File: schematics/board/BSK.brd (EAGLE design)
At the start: 80 x 80 mm, 58 parts, among them IC2 MAX809REUR, J1 idc_2x5, SW1 RST

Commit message: изменен БСК4
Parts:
- removed R2, R7: 10k, resistor:R0603
- removed U$16: FS8205A, CanCubeSat:FS8205A
- VAR3: device pinheadCS:1X12 -> pinheadCS:1X14
- moved VAR3 111.5 mm to (-80.0, -743.0)
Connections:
- removed net N$4: R2.2, U$16.4
- removed net N$6: R7.2, U$16.5
- removed net PL-: U$16.2, U$16.3, VAR3.1
- removed net SCL: U$13.30, VAR3.11
- removed net SDA: U$13.31, VAR3.12
- new net I2CINT: VAR3.5
- new net SCLTM: U$13.30, VAR3.7
- new net SDATM: U$13.31, VAR3.6
- new net TIME: VAR3.4
- net 1W: now also VAR3.14; no longer VAR3.8
- net 5V: now also VAR3.2; no longer VAR3.9
- net BUS+: now also VAR3.3; no longer VAR3.10
- net GND: now also VAR3.9; no longer U$16.6, U$16.7, VAR3.3
- net KEM10: now also VAR3.10; no longer VAR3.4
- net KEM9: now also VAR3.11; no longer VAR3.5
- net KHEAT5: now also VAR3.12; no longer VAR3.6
- net KVCC5: now also VAR3.13; no longer VAR3.7
- net VCCL: now also VAR3.8; no longer R2.1, R7.1
- net VDD: now also VAR3.1; no longer VAR3.2

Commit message: изменен БСК1
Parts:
- removed C3, C4: 100nF, rcl:C0603
- removed D1, D2: (no value), display-hp:HLMP6
- removed IC2: MAX809REUR, MAX809_:SOT23
- removed J1: idc_2x5, idc_2x5:CNC_3221-10-0100-00
- removed R21, R22, R23, R24, R25: 10k, resistor-shunt:BVS
- removed R26: 10k\, resistor-shunt:BVS
- removed R5, R6: 2k, resistor-shunt:BVS
- removed SW1: RST, 1437566-3:SW_1437566-3
- added C2, C7: 10µ, rcl:C0603
- added C33: 0,1µ, rcl:C0603
- added R1: 510k, resistor:R0603
- added U$16: USB-C, CanCubeSat:USB-C
- moved VAR3 839.2 mm to (47.0, 86.6), turned to 180 degrees
- moved VAR1A 796.6 mm to (7.40, 53.0), turned to 270 degrees
- moved U$21 768.6 mm to (63.3, 30.7), turned to 225 degrees
- moved VAR1 751.3 mm to (41.0, 7.40)
- moved U$20 748.5 mm to (71.7, 22.3), turned to 225 degrees
- moved U$4 745.8 mm to (63.3, 63.3), turned to 315 degrees
- moved U$3 742.3 mm to (71.7, 71.7), turned to 315 degrees
- moved U$19 735.0 mm to (30.7, 30.7), turned to 135 degrees
- moved U$1 716.3 mm to (22.3, 71.7), turned to 45 degrees
- moved U$18 711.5 mm to (22.3, 22.3), turned to 135 degrees
- moved U$2 710.8 mm to (30.7, 63.3), turned to 45 degrees
- moved VAR2 691.2 mm to (86.6, 47.0), turned to 90 degrees
- moved R11 543.1 mm to (79.6, 43.2), turned to 270 degrees
- moved R19 537.4 mm to (81.8, 43.3), turned to 270 degrees
- moved R10 537.0 mm to (75.3, 43.2), turned to 270 degrees
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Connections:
- removed net N$17: D1.K, R5.2
- removed net N$18: D2.K, R6.1
- removed net N$21: C4.1, IC2.2, R21.2, SJ1.2, SW1.2, U$13.3
- removed net N$23: J1.4, R23.2, U$13.13
- removed net N$26: J1.8, R25.2, U$13.14
- removed net N$27: J1.6, R24.2, U$13.23
- removed net N$29: J1.10, R26.1, SJ1.1
- removed net VDD3: D2.A, U$13.8
- new net N$44: U$16.P$12, U$16.P$9
- new net N$45: U$16.P$10
- new net N$46: U$16.P$2, U$16.P$7
- new net N$47: U$16.P$11
- new net N$48: U$16.P$6
- new net N$49: U$16.P$5
- new net N$50: U$16.P$4
- new net N$55: SJ1.2, U$13.25
- net GND: now also C2.2, C33.2, C7.2, SJ1.1; no longer C3.2, C4.2, IC2.1, J1.3, J1.7, J1.9, R5.1, SW1.1
- net N$22: now also C7.1, R1.2, U$13.3; no longer J1.2, R22.2, U$13.16
- net VDD: now also C2.1, C33.1, R1.1; no longer C3.1, D1.A, IC2.3, J1.1, R21.1, R22.1, R23.1, R24.1, R25.1, R26.2, R6.2
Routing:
- added copper zone on layer 1, net HEAT
- added copper zone on layer 1, net HEAT1
- added copper zone on layer 1, net HEAT2
- added copper zone on layer 1, net HEAT3
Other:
- board size 80 x 80 mm -> 94 x 94 mm
- board text added: "BSK1 "Концерн ИТС""
- board text added: "BUS+"
- board text added: "BUS-"

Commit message: доработана схема БСК1
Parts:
- removed SJ1: (no value), jumper:SJW
- removed U$14: FS8205A, CanCubeSat:FS8205A
- added R2: 5k, resistor:R0603
- added U$22: FS8205A+, CanCubeSat:FS8205A+
- C7: value 10µ -> 1nF
- R1: value 510k -> 12k
- U$5: value DS18B20ZDS18B20Z -> DS18B20Z
- moved C7 805.7 mm to (64.0, 78.9), turned to 180 degrees
- moved C2 796.6 mm to (64.0, 74.7), turned to 180 degrees
- moved C33 793.8 mm to (64.0, 76.8), turned to 180 degrees
- moved R1 756.1 mm to (49.8, 26.0), turned to 270 degrees
- moved U$17 544.3 mm to (77.5, 32.9)
- moved U$15 521.8 mm to (13.5, 31.2)
- moved U$9 486.8 mm to (33.5, 15.5)
- moved U$11 418.8 mm to (53.8, 26.0), turned to 270 degrees
- moved U$12 411.2 mm to (50.4, 15.3), turned to 270 degrees
- moved C13 404.7 mm to (42.6, 19.8), turned to 180 degrees
- moved C9 395.4 mm to (44.6, 16.1), turned to 90 degrees
- moved C6 391.5 mm to (50.2, 23.2), turned to 180 degrees
- moved C15 387.0 mm to (49.7, 12.3)
- moved C14 382.3 mm to (42.7, 22.0)
- moved R13 376.7 mm to (51.9, 26.0), turned to 270 degrees
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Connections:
- removed net N$22: C7.1, R1.2, U$13.3
- removed net N$44: U$16.P$12, U$16.P$9
- removed net N$45: U$16.P$10
- removed net N$46: U$16.P$2, U$16.P$7
- removed net N$47: U$16.P$11
- removed net N$48: U$16.P$6
- removed net N$49: U$16.P$5
- removed net N$50: U$16.P$4
- removed net N$55: SJ1.2, U$13.25
- new net BUS+1: U$1.1, U$1.2, U$1.3, U$1.4, U$1.P$1, U$1.P$2
- new net BUS+2: U$18.1, U$18.2, U$18.3, U$18.4, U$18.P$1, U$18.P$2
- new net BUS+3: U$20.1, U$20.2, U$20.3, U$20.4, U$20.P$1, U$20.P$2
- new net BUS-1: U$4.1, U$4.2, U$4.3, U$4.4, U$4.P$1, U$4.P$2
- new net BUS-2: U$19.1, U$19.2, U$19.3, U$19.4, U$19.P$1, U$19.P$2
- new net BUS-3: U$21.1, U$21.2, U$21.3, U$21.4, U$21.P$1, U$21.P$2
- new net EN: C7.1, R1.1, U$13.3, U$16.RESET/EN
- new net HEAT: U$10.HEAT, U$13.HEAT, U$22.HEAT, U$5.HEAT, U$8.HEAT
- new net IO0: R2.1, U$13.25, U$16.GPIO
- new net RX-C: U$13.34, U$16.SWD/RXD
- new net TX-C: U$13.35, U$16.SWC/TXD
- net BUS+: now also U$16.NC/BUS0, U$16.NC/BUS1; no longer U$1.1, U$1.2, U$1.3, U$1.4, U$1.P$1, U$1.P$2, U$18.1, U$18.2, U$18.3, U$18.4, U$18.P$1, U$18.P$2, U$20.1, U$20.2, U$20.3, U$20.4, U$20.P$1, U$20.P$2
- net BUS-: now also U$22.23; no longer U$14.2, U$14.3, U$19.1, U$19.2, U$19.3, U$19.4, U$19.P$1, U$19.P$2, U$21.1, U$21.2, U$21.3, U$21.4, U$21.P$1, U$21.P$2, U$4.1, U$4.2, U$4.3, U$4.4, U$4.P$1, U$4.P$2
- net GND: now also U$13.32, U$16.GND0, U$16.GND1, U$22.67; no longer SJ1.1, U$10.P$1, U$13.P$39, U$13.P$40, U$13.P$41, U$13.P$42, U$13.P$43, U$13.P$44, U$13.P$45, U$13.P$46, U$13.P$47, U$14.6, U$14.7
- net KEM10: now also U$17.7
- net KEM7: no longer U$17.6
- net KEM8: no longer U$17.7
- net KEM9: now also U$17.6
- net N$8: now also U$22.4; no longer U$14.4
- net N$9: now also U$22.5; no longer U$14.5
- net VDD: now also R1.2, R2.2; no longer R1.1
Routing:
- net GND: track 0.00 -> 361.0 mm, vias 0 -> 19
- net 5V: track 0.00 -> 328.7 mm, vias 0 -> 16
- net BUS+: track 0.00 -> 269.3 mm, vias 0 -> 13
- net 1W: track 0.00 -> 256.0 mm, vias 0 -> 9
- net VDD: track 0.00 -> 227.8 mm, vias 0 -> 13
- net SHCP: track 0.00 -> 195.3 mm, vias 0 -> 11
- net STCP: track 0.00 -> 193.7 mm, vias 0 -> 14
- net EN: track 0.00 -> 188.6 mm, vias 0 -> 7
- net KEM6: track 0.00 -> 177.1 mm, vias 0 -> 5
- net IN1: track 0.00 -> 176.5 mm, vias 0 -> 10
- net IO0: track 0.00 -> 176.4 mm, vias 0 -> 7
- net KVCC5: track 0.00 -> 158.8 mm, vias 0 -> 9
- net HEAT: track 0.00 -> 148.7 mm
- net IN2: track 0.00 -> 146.7 mm, vias 0 -> 4
- net RX-C: track 0.00 -> 141.4 mm, vias 0 -> 2
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
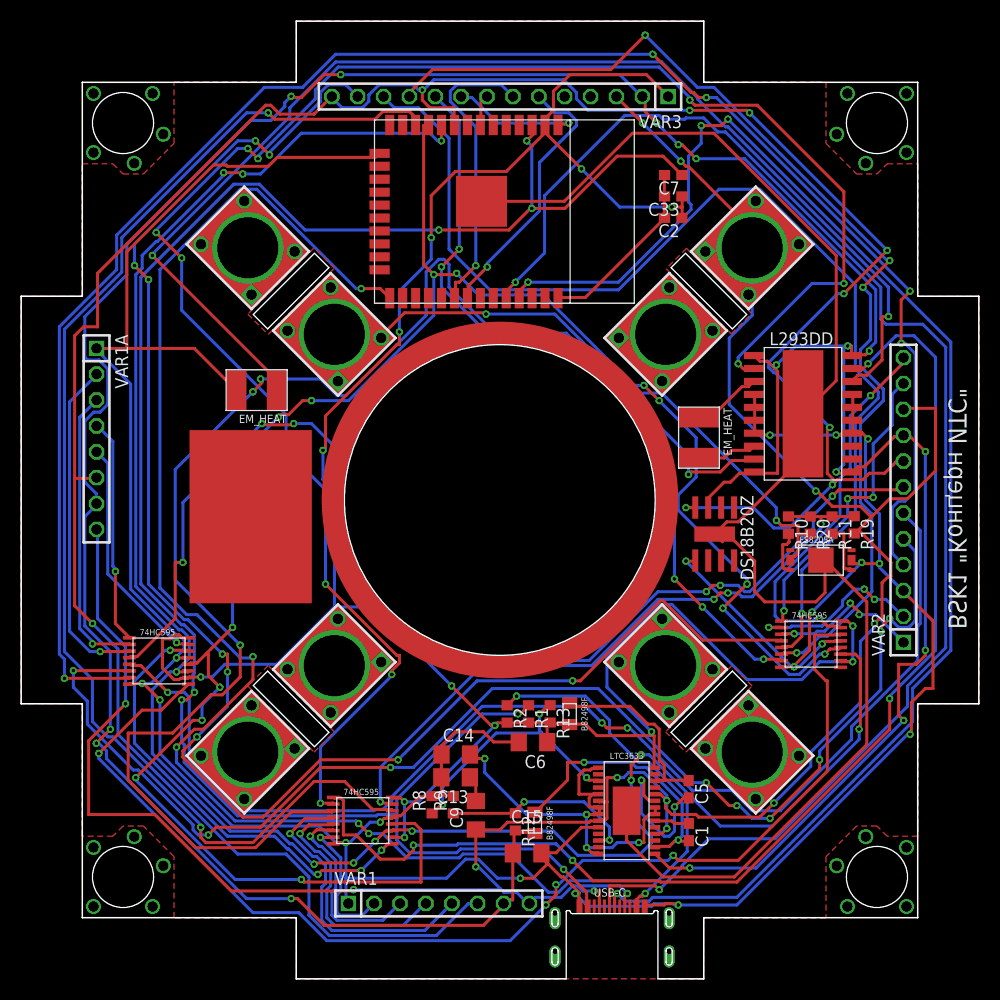
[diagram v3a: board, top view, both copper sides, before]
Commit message: Реструктурированы сигналы коммутации для плат БСК
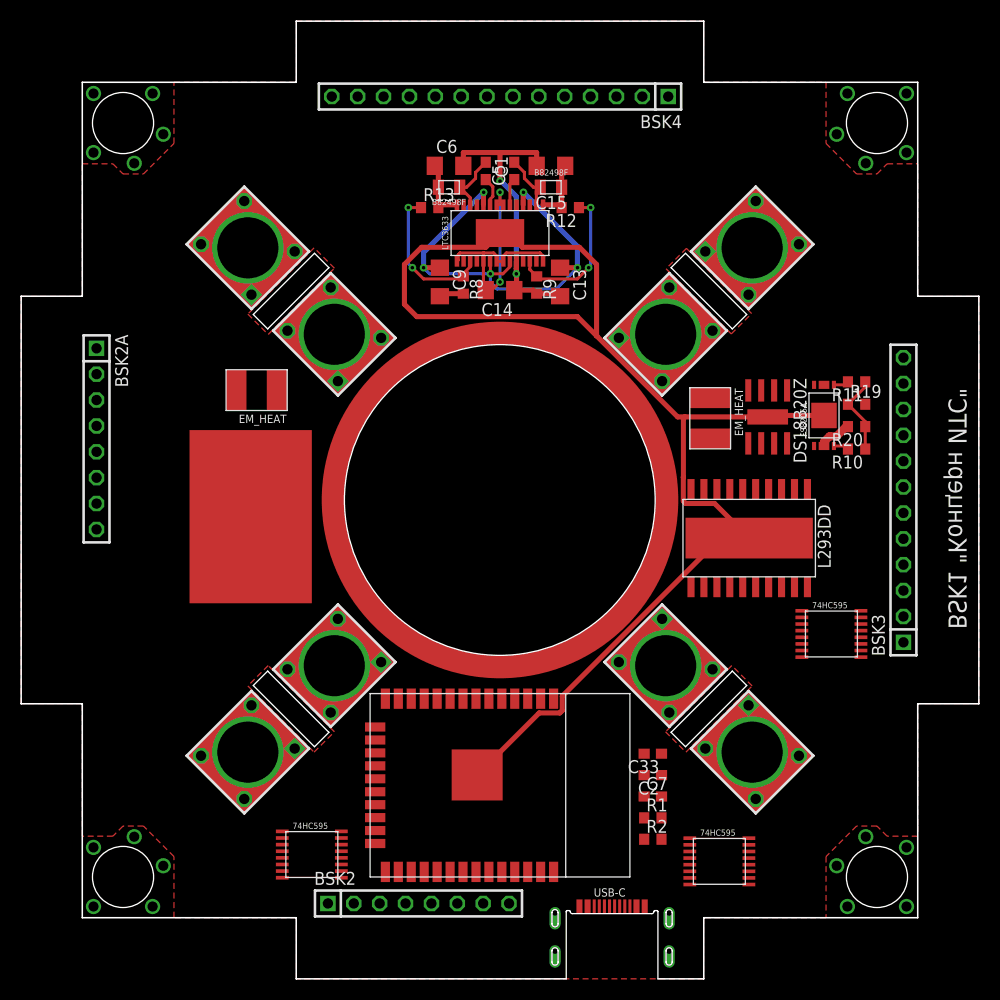
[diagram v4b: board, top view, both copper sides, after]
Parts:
- removed VAR1: (no value), pinheadCS:1X08
- added BSK2: (no value), pinheadCS:1X08
- moved C15 67.5 mm to (52.0, 79.8), turned to 180 degrees
- moved C1 67.1 mm to (48.4, 79.3), turned to 90 degrees
- moved C5 63.9 mm to (45.6, 79.3)
- moved U$12 62.4 mm to (52.0, 77.7), turned to 0 degrees
- moved C7 61.0 mm to (62.0, 17.9), turned to 0 degrees
- moved R12 60.5 mm to (53.9, 75.7), turned to 180 degrees
- moved U$10 58.0 mm to (47.0, 73.2), turned to 0 degrees
- moved C6 57.2 mm to (42.0, 79.8), turned to 0 degrees
- moved U$13 56.3 mm to (47.0, 19.0)
- moved C2 54.7 mm to (62.0, 20.0)
- moved C33 54.7 mm to (62.0, 22.1)
- moved U$11 53.0 mm to (42.0, 77.7), turned to 180 degrees
- moved C9 52.5 mm to (41.1, 68.4), turned to 270 degrees
- moved R9 51.7 mm to (50.6, 68.1), turned to 270 degrees
- moved R8 51.1 mm to (43.4, 68.1), turned to 270 degrees
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- renumbered VAR1A to BSK2A, VAR2 to BSK3, VAR3 to BSK4
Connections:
- net IN1 renamed B1_KEM+
- net IN2 renamed B1_KEM-
- net IN4 renamed B1_KHEAT
- net KEM3 renamed B2A_KEM+
- net KEM4 renamed B2A_KEM-
- net KEM7 renamed B5_KEM+
- net KEM8 renamed B5_KEM-
- net KHEAT2 renamed B2A_KHEAT
- net KHEAT4 renamed B5_KHEAT
- net KVCC0 renamed B1_KVCC
- net KVCC2 renamed B2A_KVCC
- net KVCC4 renamed B5_KVCC
- net VCCL renamed PL_KVCC
- removed net KEM1: U$9.6, VAR1.3
- removed net KEM10: BSK4.10, U$17.7
- removed net KEM2: U$9.7, VAR1.2
- removed net KEM5: BSK3.5, U$15.6
- removed net KEM6: BSK3.4, U$15.7
- removed net KEM9: BSK4.11, U$17.6
- removed net KHEAT1: U$9.5, VAR1.4
- removed net KHEAT3: BSK3.6, U$15.5
- removed net KHEAT5: BSK4.12, U$17.5
- removed net KVCC1: U$9.4, VAR1.5
- removed net KVCC3: BSK3.7, U$15.4
- removed net KVCC5: BSK4.13, U$17.4
- removed net N$36: C13.1, C9.2
- new net B2_KEM+: BSK2.3, U$9.6
- new net B2_KEM-: BSK2.2, U$9.7
- new net B2_KHEAT: BSK2.4, U$9.5
- new net B2_KVCC: BSK2.5, U$9.4
- new net B3_KEM+: BSK3.5, U$17.6
- new net B3_KEM-: BSK3.4, U$17.7
- new net B3_KHEAT: BSK3.6, U$17.5
- new net B3_KVCC: BSK3.7, U$17.4
- new net B4_KEM+: BSK4.11, U$15.6
- new net B4_KEM-: BSK4.10, U$15.7
- new net B4_KHEAT: BSK4.12, U$15.5
- new net B4_KVCC: BSK4.13, U$15.4
- net 1W: now also BSK2.6; no longer VAR1.6
- net 5V: now also BSK2.7; no longer VAR1.7
- net BUS+: now also BSK2.8, C13.1; no longer VAR1.8
- net GND: now also BSK2.1, C9.2; no longer VAR1.1
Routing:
- net GND: track 361.0 -> 32.5 mm, vias 19 -> 2
- net 5V: track 328.7 -> 6.60 mm, vias 16 -> 0
- net 1W: track 256.0 -> 0.00 mm, vias 9 -> 0
- net BUS+: track 269.3 -> 46.5 mm, vias 13 -> 5
- net VDD: track 227.8 -> 6.37 mm, vias 13 -> 0
- net SHCP: track 195.3 -> 0.00 mm, vias 11 -> 0
- net STCP: track 193.7 -> 0.00 mm, vias 14 -> 0
- net EN: track 188.6 -> 0.00 mm, vias 7 -> 0
- net KEM6: track 177.1 -> 0.00 mm, vias 5 -> 0
- net B1_KEM+: track 176.5 -> 0.00 mm, vias 10 -> 0
- net IO0: track 176.4 -> 0.00 mm, vias 7 -> 0
- net KVCC5: track 158.8 -> 0.00 mm, vias 9 -> 0
- net B1_KEM-: track 146.7 -> 0.00 mm, vias 4 -> 0
- net RX-C: track 141.4 -> 0.00 mm, vias 2 -> 0
- net TX-C: track 140.5 -> 0.00 mm, vias 4 -> 0
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
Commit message: доработаны схемы БСК1 и БКУ
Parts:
- added LED1: (no value), led:CHIPLED_0603
- added R3: 2k, resistor:R0603
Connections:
- removed net HEAT: U$10.HEAT, U$13.HEAT, U$22.HEAT, U$5.HEAT, U$8.HEAT
- new net IO1: R3.1, U$13.30
- new net N$34: LED1.C, R3.2
- net 1W: now also U$13.33; no longer U$13.9
- net BUS+: now also U$16.3V3/BUS0, U$16.3V3/BUS1; no longer U$16.NC/BUS0, U$16.NC/BUS1
- net EN: now also U$16.NRST/EN; no longer U$16.RESET/EN
- net GND: now also U$10.HEAT, U$13.HEAT, U$22.HEAT, U$5.HEAT, U$8.HEAT
- net I2CINT: now also U$13.29
- net IO0: now also U$16.NC/GPIO; no longer U$16.GPIO
- net PL_KVCC: now also U$13.9; no longer U$13.7
- net SCLTM: now also U$13.27; no longer U$13.30
- net SDATM: now also U$13.28; no longer U$13.31
- net TIME: now also U$13.31
- net VDD: now also LED1.A
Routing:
- net HEAT: track 129.4 -> 0.00 mm
- net GND: track 32.5 -> 161.9 mm
- added copper zone on layer 1, net GND
- removed copper zone on layer 1, net HEAT
